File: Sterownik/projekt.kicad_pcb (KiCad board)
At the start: 2 copper layers, 72.4 x 45.7 mm, 65 parts, among them P1 CONN_01X08, P3 CONN_01X05, P4 CONN_01X02, P5 CONN_01X02, P6 USB_OTG, P8 CONN_01X02, SW1 SW_PUSH_SMALL, T10 Si2323DS, T12 2N7002, T18 2N7002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

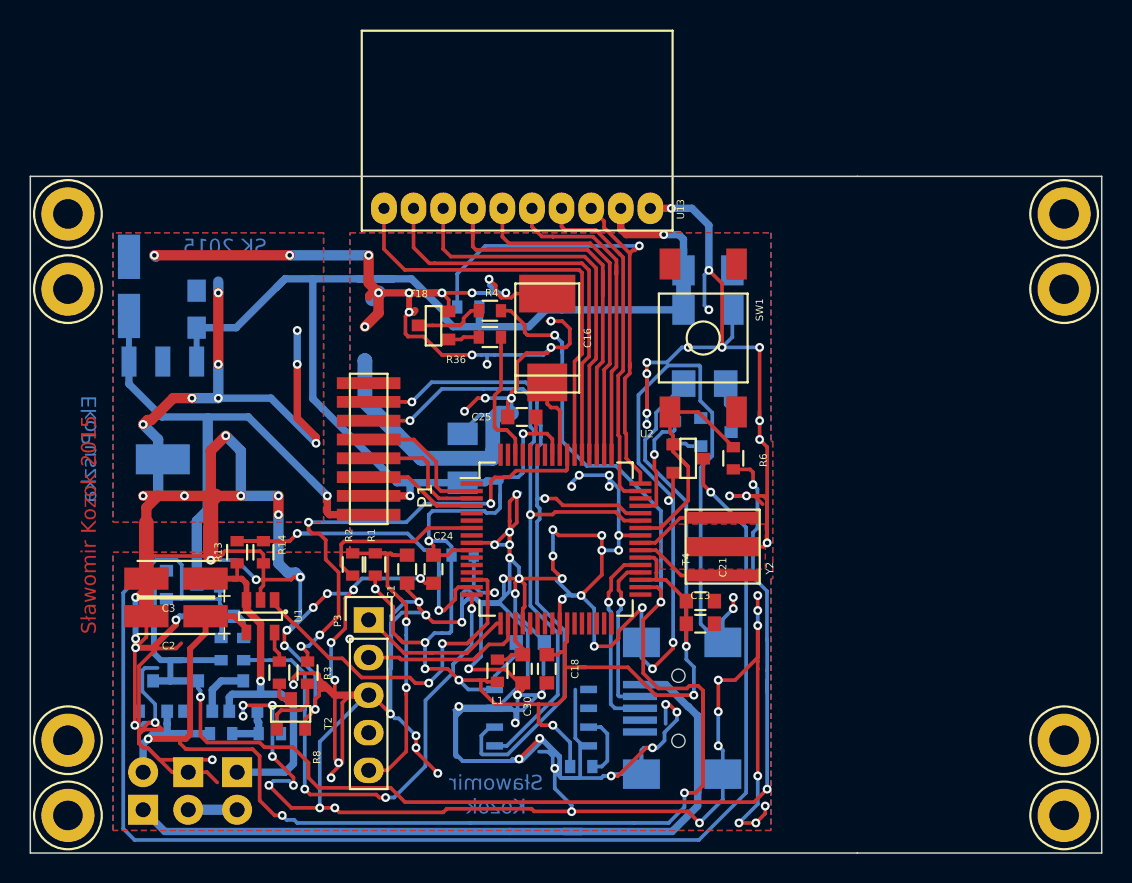
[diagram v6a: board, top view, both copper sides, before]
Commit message: Changed switch placement (from main to sensor board)
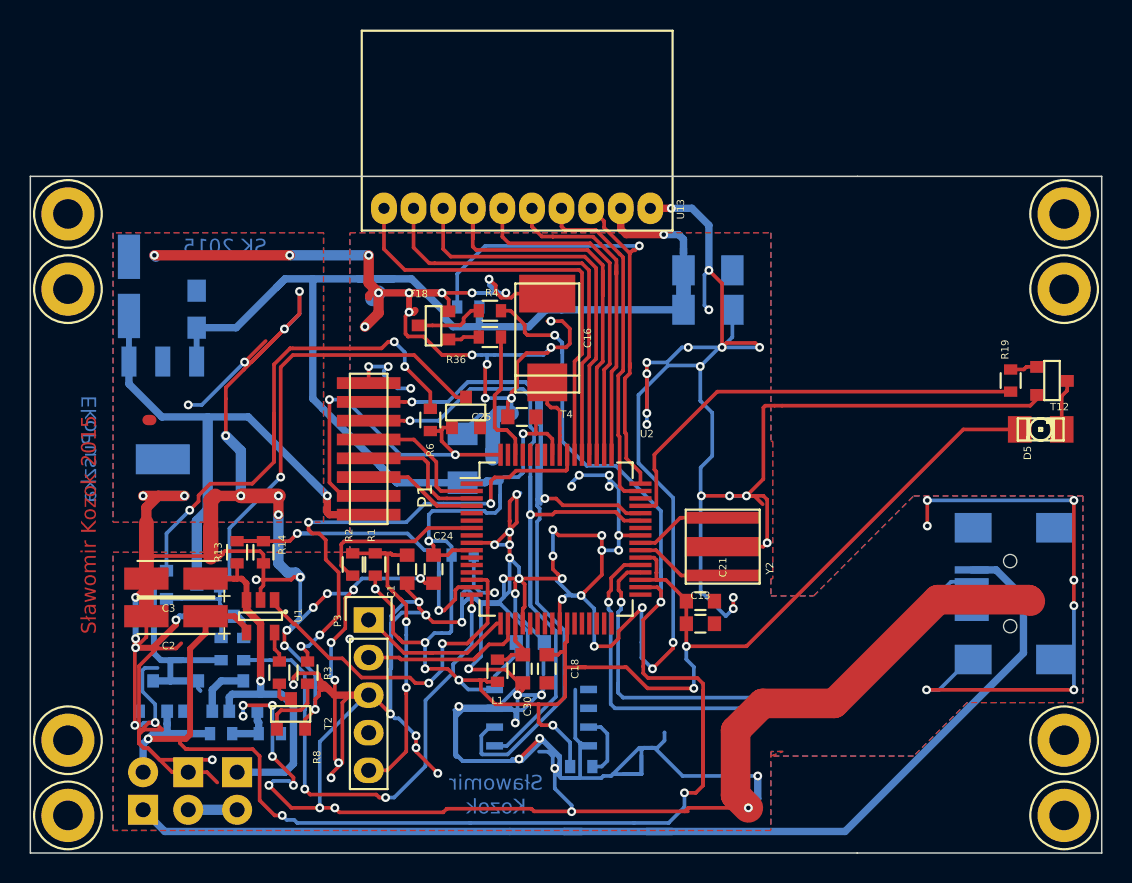
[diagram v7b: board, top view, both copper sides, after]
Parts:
- removed SW1: SW_PUSH_SMALL, Footprinty:TACT_SW_ONE_PAIR
- D5, R19, T12: moved to F.Cu
- moved P6 23.7 mm to (244.9, 108.3)
- moved R19 23.0 mm to (244.0, 93.9), turned to 270 degrees
- moved T12 23.0 mm to (246.8, 93.9), turned to 270 degrees
- moved D5 22.9 mm to (246.1, 97.2)
- moved R6 20.6 mm to (204.8, 96.6), turned to 270 degrees
- moved T4 15.4 mm to (207.2, 96.1), turned to 0 degrees
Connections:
- net VON renamed VINPUT
- P1 pad 2: VDD -> TERMINATE
- U2 pad 42: TERMINATE -> (no net)
- U2 pad 64: (no net) -> TERMINATE
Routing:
- net ON_BUT: track 98.0 -> 37.8 mm
- net VINPUT: track 89.2 -> 57.5 mm
- net GND: track 717.9 -> 746.5 mm, vias 136 -> 126
- net DATA-: track 12.0 -> 37.1 mm
- net DATA+: track 14.0 -> 38.7 mm
- net POWER_LED: track 7.77 -> 30.4 mm, vias 1 -> 0
- net SCL: track 51.1 -> 72.9 mm
- net VUSB_BUS: track 56.0 -> 76.0 mm
- net TERMINATE: track 16.6 -> 25.5 mm, vias 0 -> 2
- net SDA: track 46.6 -> 55.2 mm
- net VDD: track 195.0 -> 200.9 mm, vias 11 -> 10
